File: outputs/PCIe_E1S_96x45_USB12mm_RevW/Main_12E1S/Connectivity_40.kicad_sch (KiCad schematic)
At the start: 12 parts

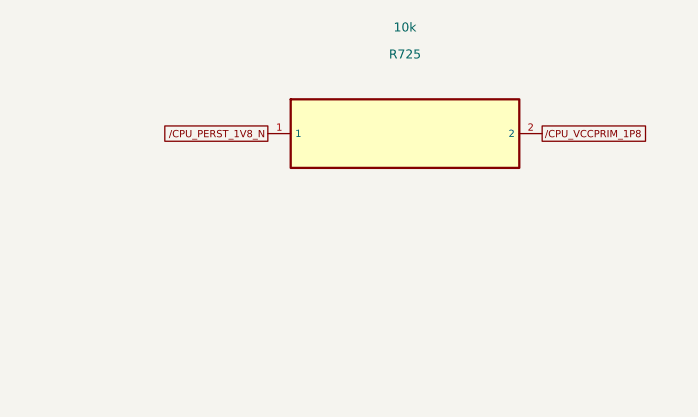
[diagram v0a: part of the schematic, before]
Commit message: Rebuild E1S reset routing and remove conflicting PLTRST pull-up
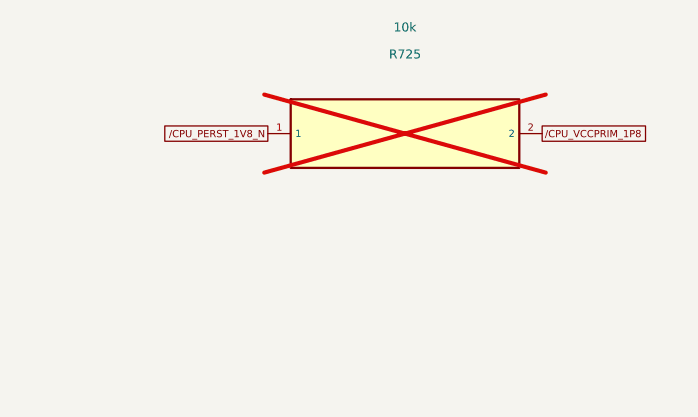
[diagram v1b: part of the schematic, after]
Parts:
- R725: now not fitted
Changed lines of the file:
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@@
 (global_label "/PEX_SYS_RESET_N" (shape passive) (at 345.44 73.66 180) (effects (font (size 0.8 0.8)) (justify right)))
 (global_label "/PEX_1V8" (shape passive) (at 375.92 73.66 0) (effects (font (size 0.8 0.8)) (justify left)))
-(symbol (lib_id "Local:PART_R725") (at 504.19 73.66 0) (unit 1) (in_bom yes) (on_board yes) (dnp no) (property "Reference" "R725" (at 504.19 64.85 0) (effects (font (size 1 1))))(property "Value" "10k" (at 504.19 61.849999999999994 0) (effects (font (size 1 1))))(property "Footprint" "Local:R_0402_1005Metric" (at 504.19 73.66 0) (effects (font (size 1 1)) (hide yes)))(pin "1")(pin "2")(instances (project "Main_12E1S" (path "/c33a6c5d-1a9e-4453-a37d-d3058a6ae0e3/4ea1d9c7-472e-4529-b4d4-10642039907a" (reference "R725") (unit 1)))))
+(symbol (lib_id "Local:PART_R725") (at 504.19 73.66 0) (unit 1) (in_bom yes) (on_board yes) (dnp yes) (property "Reference" "R725" (at 504.19 64.85 0) (effects (font (size 1 1))))(property "Value" "10k" (at 504.19 61.849999999999994 0) (effects (font (size 1 1))))(property "Footprint" "Local:R_0402_1005Metric" (at 504.19 73.66 0) (effects (font (size 1 1)) (hide yes)))(pin "1")(pin "2")(instances (project "Main_12E1S" (path "/c33a6c5d-1a9e-4453-a37d-d3058a6ae0e3/4ea1d9c7-472e-4529-b4d4-10642039907a" (reference "R725") (unit 1)))))
 (global_label "/CPU_PERST_1V8_N" (shape passive) (at 488.95 73.66 180) (effects (font (size 0.8 0.8)) (justify right)))
 (global_label "/CPU_VCCPRIM_1P8" (shape passive) (at 519.43 73.66 0) (effects (font (size 0.8 0.8)) (justify left)))

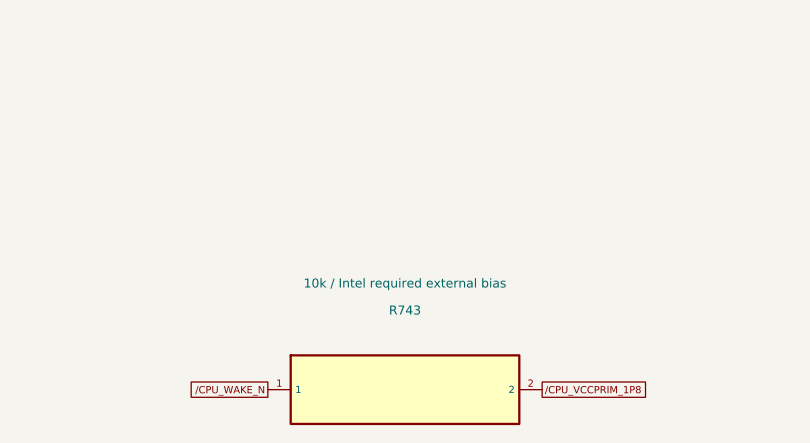
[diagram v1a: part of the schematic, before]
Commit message: Set R743 WAKE bias to conservative 4.7k 1 percent
Synchronize six design representations with eight R743-only value substitutions, preserving original line endings. Cover possible enabled 15k internal pull-down without claiming 10k fails every state; preserve the TERM none discrepancy. Independent byte guards, replay, refill, native DRC/ERC and electrical margin checks are recorded. All copper and fills are unchanged; physical WAKE and driver/power qualification remain incomplete.
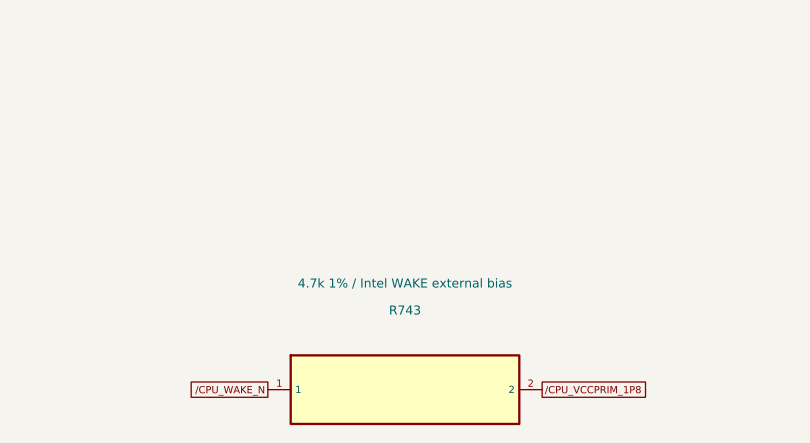
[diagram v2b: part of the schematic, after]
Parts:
- R743: value 10k / Intel required external bias -> 4.7k 1% / Intel WAKE external bias
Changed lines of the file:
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@@
 (global_label "/CPU_PMCALERT_N" (shape passive) (at 203.2 330.2 180) (effects (font (size 0.8 0.8)) (justify right)))
 (global_label "/CPU_VCCPRIM_1P8" (shape passive) (at 233.68 330.2 0) (effects (font (size 0.8 0.8)) (justify left)))
-(symbol (lib_id "Local:PART_R743") (at 360.68 330.2 0) (unit 1) (in_bom yes) (on_board yes) (dnp no) (property "Reference" "R743" (at 360.68 321.39 0) (effects (font (size 1 1))))(property "Value" "10k / Intel required external bias" (at 360.68 318.39 0) (effects (font (size 1 1))))(property "Footprint" "Local:R_0402_1005Metric" (at 360.68 330.2 0) (effects (font (size 1 1)) (hide yes)))(pin "1")(pin "2")(instances (project "Main_12E1S" (path "/c33a6c5d-1a9e-4453-a37d-d3058a6ae0e3/4ea1d9c7-472e-4529-b4d4-10642039907a" (reference "R743") (unit 1)))))
+(symbol (lib_id "Local:PART_R743") (at 360.68 330.2 0) (unit 1) (in_bom yes) (on_board yes) (dnp no) (property "Reference" "R743" (at 360.68 321.39 0) (effects (font (size 1 1))))(property "Value" "4.7k 1% / Intel WAKE external bias" (at 360.68 318.39 0) (effects (font (size 1 1))))(property "Footprint" "Local:R_0402_1005Metric" (at 360.68 330.2 0) (effects (font (size 1 1)) (hide yes)))(pin "1")(pin "2")(instances (project "Main_12E1S" (path "/c33a6c5d-1a9e-4453-a37d-d3058a6ae0e3/4ea1d9c7-472e-4529-b4d4-10642039907a" (reference "R743") (unit 1)))))
 (global_label "/CPU_WAKE_N" (shape passive) (at 345.44 330.2 180) (effects (font (size 0.8 0.8)) (justify right)))
 (global_label "/CPU_VCCPRIM_1P8" (shape passive) (at 375.92 330.2 0) (effects (font (size 0.8 0.8)) (justify left)))
